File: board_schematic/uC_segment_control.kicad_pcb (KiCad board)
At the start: 2 copper layers, 139 x 94 mm, 140 parts, among them IC101 ATMEGA88PA-P, P101 CONN_01X03, P102 CONN_01X03, P103 CONN_01X03, P104 CONN_01X03, P105 CONN_01X03, P106 CONN_01X03, P107 CONN_01X02, P108 CONN_01X02, P109 CONN_01X02, P110 CONN_01X02, P111 CONN_01X02, P112 CONN_01X02, P113 CONN_01X02, P114 CONN_01X02, P115 CONN_01X02, P116 CONN_01X02, P117 CONN_01X02, P118 CONN_01X02, P119 CONN_01X02, P120 CONN_01X02, P121 CONN_01X03, P122 CONN_01X03, P123 CONN_01X02, P124 CONN_01X02, P125 CONN_01X02, P126 CONN_01X02, P127 CONN_01X02, P128 CONN_02X05, P129 CONN_01X02, P130 CONN_01X02, P201 CONN_01X02_P, Q1001 IRLML2244, Q1002 BC548, Q101 IRLML2502, Q102 IRLML2502, Q103 IRLML2502, Q104 IRLML2502, Q105 IRLML2502, Q106 IRLML2502, Q1101 IRLML2244, Q1102 BC548, Q1201 IRLML2244, Q1202 BC548, Q1301 IRLML2244, Q1302 BC548, Q1401 IRLML2244, Q1402 BC548, Q1501 IRLML2244, Q1502 BC548, Q1601 IRLML2244, Q1602 BC548, Q301 IRLML2244, Q302 BC548, Q401 IRLML2244, Q402 BC548, Q501 IRLML2244, Q502 BC548, Q601 IRLML2244, Q602 BC548, Q701 IRLML2244, Q702 BC548, Q801 IRLML2244, Q802 BC548, Q901 IRLML2244, Q902 BC548, U201 LF33

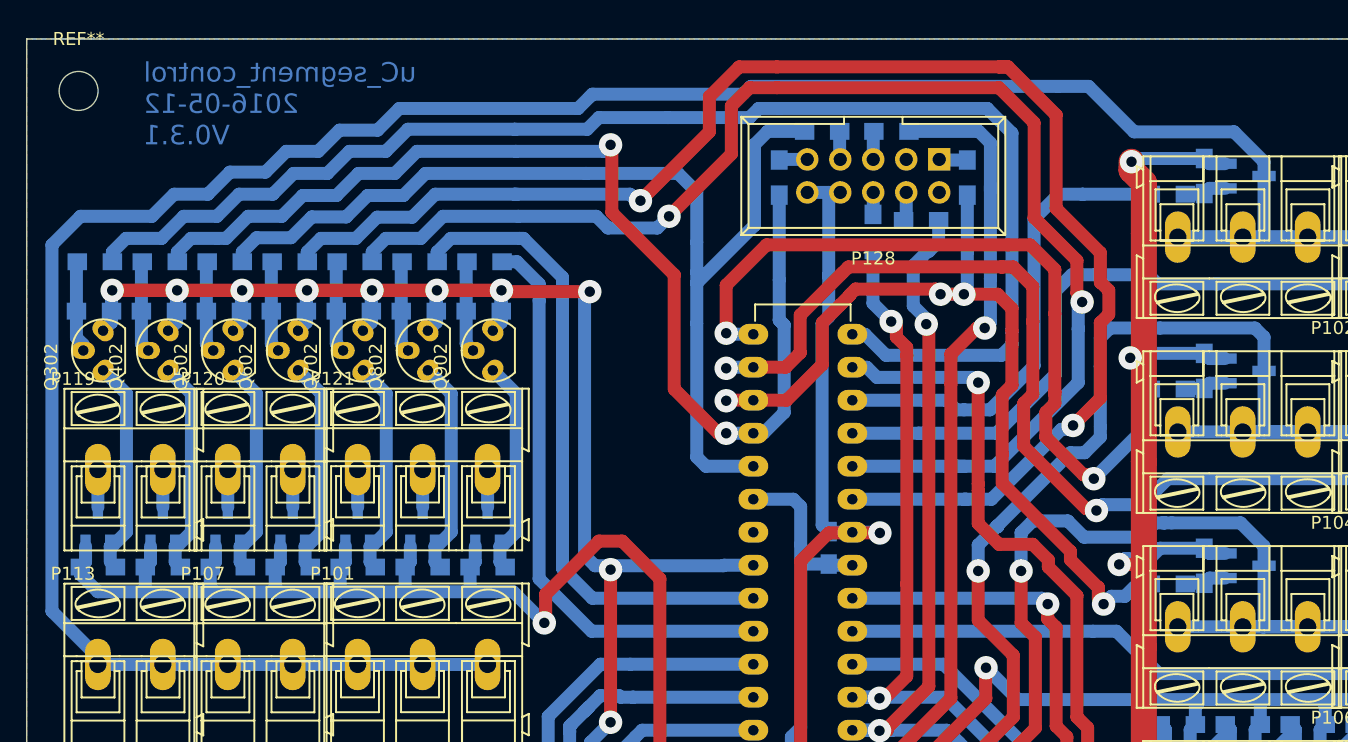
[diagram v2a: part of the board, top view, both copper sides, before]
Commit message: V0.4.1 bigger pads footprint flashport for better milling. Case added.
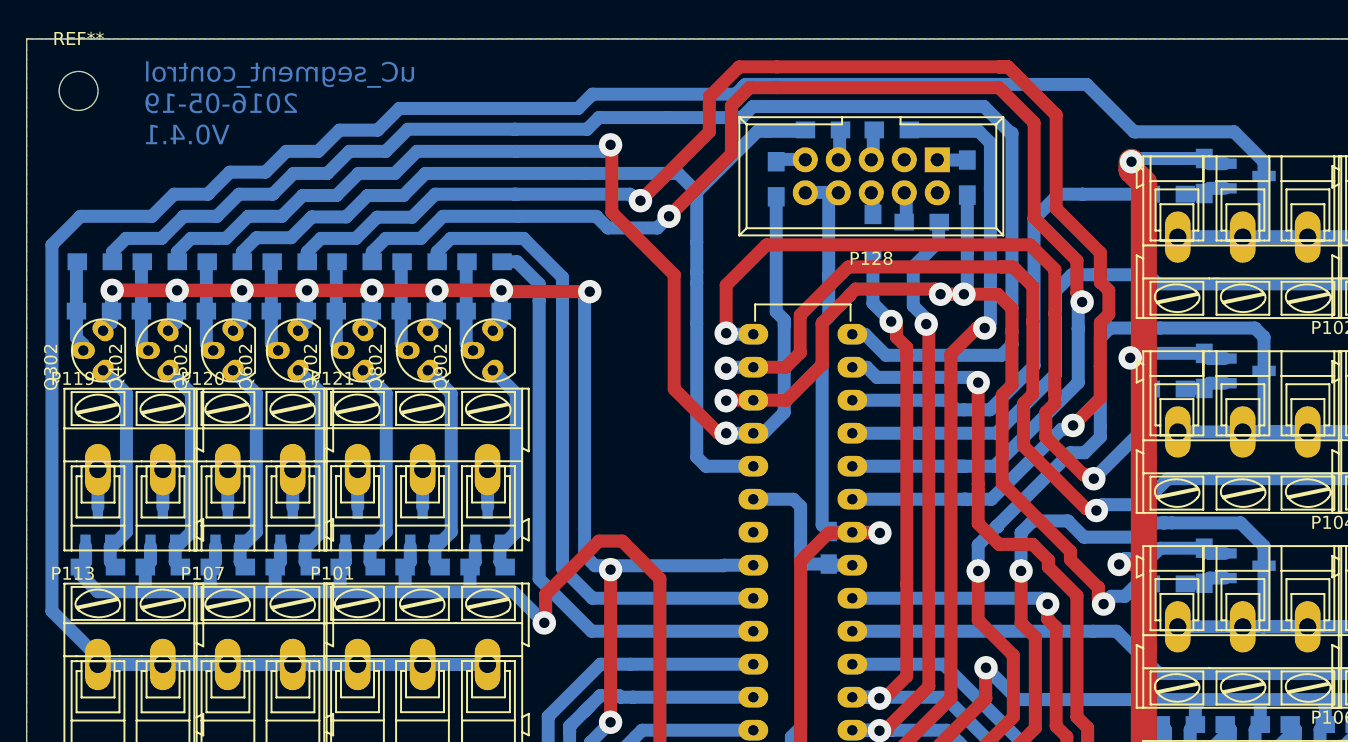
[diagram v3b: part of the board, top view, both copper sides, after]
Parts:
- P128: footprint Connect:IDC_Header_Straight_10pins -> project_footprints:IDC_Header_Straight_10pins_0.6_clearance
- moved R119 0.27 mm to (107.7, 60.8)
- moved P128 0.15 mm to (120.1, 59.3)
- moved R112 0.14 mm to (118.9, 64.1)
- moved R115 0.13 mm to (111.3, 57.0)
- moved R113 0.12 mm to (116.6, 57.0)
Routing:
- net /p-mos_switch_S0_2.sch/S_IN: track 81.5 -> 75.0 mm
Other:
- board text added: "uC_segment_control 2016-05-19 V0.4.1"
- board text removed: "uC_segment_control 2016-05-12 V0.3.1"
